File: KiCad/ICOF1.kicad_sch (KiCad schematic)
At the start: 40 parts, among them J1 USB C Connector, J2 JTAG_TC2030, SW1 Boot, U1 XC6206, U2 USBLC6-2SC6, U3 RP2040, U4 W25Q128JVS, Y1 12MHz

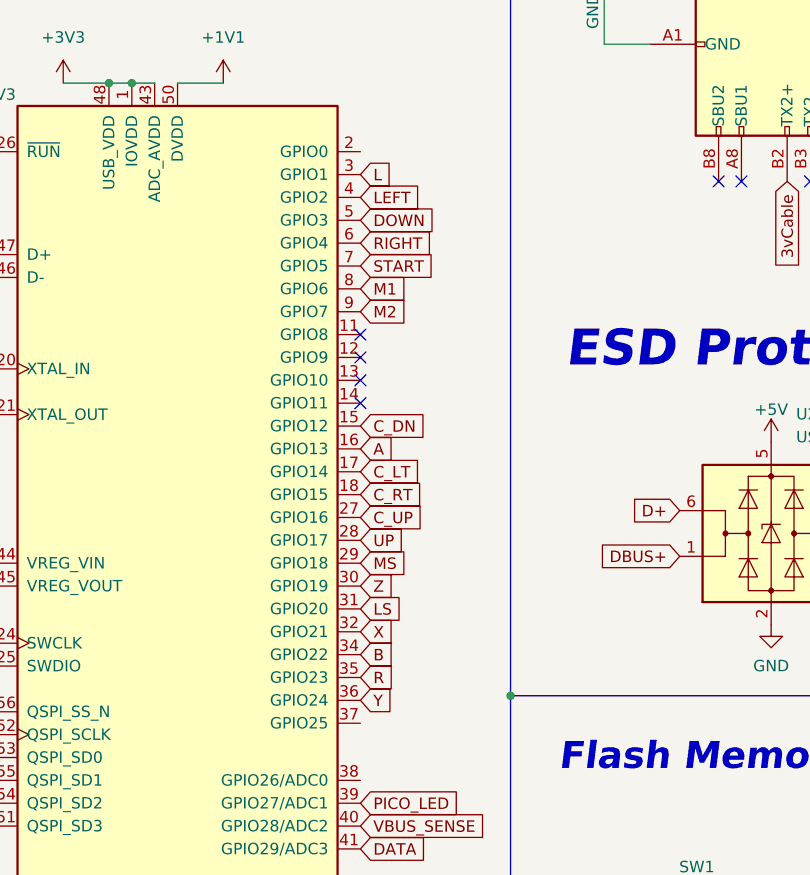
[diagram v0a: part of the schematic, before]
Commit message: fixed L and R, corrected sch pinout
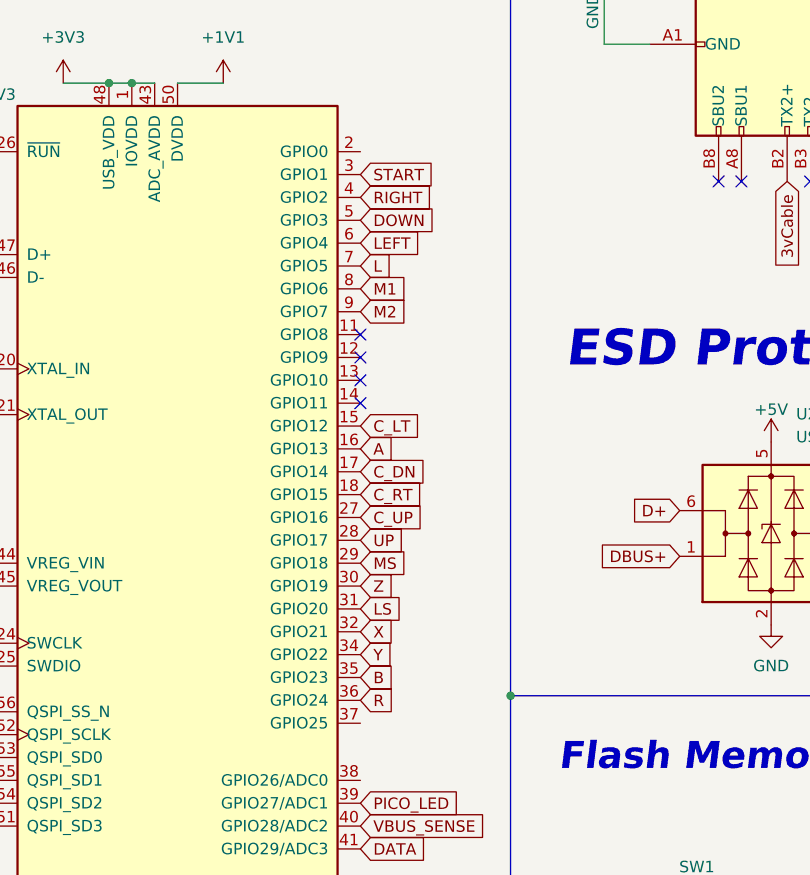
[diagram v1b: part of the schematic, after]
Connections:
- net B: now also U3.35 (GPIO23); no longer U3.34 (GPIO22)
- net C_DN: now also U3.17 (GPIO14); no longer U3.15 (GPIO12)
- net C_LT: now also U3.15 (GPIO12); no longer U3.17 (GPIO14)
- net L: now also U3.7 (GPIO5); no longer U3.3 (GPIO1)
- net LEFT: now also U3.6 (GPIO4); no longer U3.4 (GPIO2)
- net R: now also U3.36 (GPIO24); no longer U3.35 (GPIO23)
- net RIGHT: now also U3.4 (GPIO2); no longer U3.6 (GPIO4)
- net START: now also U3.3 (GPIO1); no longer U3.7 (GPIO5)
- net Y: now also U3.34 (GPIO22); no longer U3.36 (GPIO24)
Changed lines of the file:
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@@
     (effects (font (size 0.8 0.8)) (justify right bottom))
   )
-  (global_label "START" (shape input) (at 71.9648 61.214 0) (fields_autoplaced)
-    (effects (font (size 1.27 1.27)) (justify left))
-    (property "Intersheetrefs" "${INTERSHEET_REFS}" (at 79.8812 61.1346 0)
+  (global_label "L" (shape input) (at 71.9648 61.214 0) (fields_autoplaced)
+    (effects (font (size 1.27 1.27)) (justify left))
+    (property "Intersheetrefs" "${INTERSHEET_REFS}" (at 75.8987 61.214 0)
       (effects (font (size 1.27 1.27)) (justify left) hide)
     )
@@
     )
   )
-  (global_label "RIGHT" (shape input) (at 71.9648 58.674 0) (fields_autoplaced)
-    (effects (font (size 1.27 1.27)) (justify left))
-    (property "Intersheetrefs" "${INTERSHEET_REFS}" (at 79.8208 58.5946 0)
+  (global_label "LEFT" (shape input) (at 71.9648 58.674 0) (fields_autoplaced)
+    (effects (font (size 1.27 1.27)) (justify left))
+    (property "Intersheetrefs" "${INTERSHEET_REFS}" (at 79.1039 58.674 0)
       (effects (font (size 1.27 1.27)) (justify left) hide)
     )
@@
     )
   )
-  (global_label "L" (shape input) (at 71.9648 51.054 0) (fields_autoplaced)
-    (effects (font (size 1.27 1.27)) (justify left))
-    (property "Intersheetrefs" "${INTERSHEET_REFS}" (at 75.406 50.9746 0)
+  (global_label "START" (shape input) (at 71.9648 51.054 0) (fields_autoplaced)
+    (effects (font (size 1.27 1.27)) (justify left))
+    (property "Intersheetrefs" "${INTERSHEET_REFS}" (at 80.3739 51.054 0)
       (effects (font (size 1.27 1.27)) (justify left) hide)
     )
@@
     )
   )
-  (global_label "Y" (shape input) (at 71.9648 109.474 0) (fields_autoplaced)
-    (effects (font (size 1.27 1.27)) (justify left))
-    (property "Intersheetrefs" "${INTERSHEET_REFS}" (at 75.4665 109.3946 0)
+  (global_label "R" (shape input) (at 71.9648 109.474 0) (fields_autoplaced)
+    (effects (font (size 1.27 1.27)) (justify left))
+    (property "Intersheetrefs" "${INTERSHEET_REFS}" (at 76.1406 109.474 0)
       (effects (font (size 1.27 1.27)) (justify left) hide)
     )
@@
     )
   )
-  (global_label "C_DN" (shape input) (at 71.9648 78.994 0) (fields_autoplaced)
-    (effects (font (size 1.27 1.27)) (justify left))
-    (property "Intersheetrefs" "${INTERSHEET_REFS}" (at 79.216 78.9146 0)
-      (effects (font (size 1.27 1.27)) (justify left) hide)
-    )
-  )
-  (global_label "R" (shape input) (at 71.9648 106.934 0) (fields_autoplaced)
-    (effects (font (size 1.27 1.27)) (justify left))
-    (property "Intersheetrefs" "${INTERSHEET_REFS}" (at 75.6479 106.8546 0)
+  (global_label "C_LT" (shape input) (at 71.9648 78.994 0) (fields_autoplaced)
+    (effects (font (size 1.27 1.27)) (justify left))
+    (property "Intersheetrefs" "${INTERSHEET_REFS}" (at 79.1039 78.994 0)
+      (effects (font (size 1.27 1.27)) (justify left) hide)
+    )
+  )
+  (global_label "B" (shape input) (at 71.9648 106.934 0) (fields_autoplaced)
+    (effects (font (size 1.27 1.27)) (justify left))
+    (property "Intersheetrefs" "${INTERSHEET_REFS}" (at 76.1406 106.934 0)
       (effects (font (size 1.27 1.27)) (justify left) hide)
     )
@@
     )
   )
-  (global_label "LEFT" (shape input) (at 71.9648 53.594 0) (fields_autoplaced)
-    (effects (font (size 1.27 1.27)) (justify left))
-    (property "Intersheetrefs" "${INTERSHEET_REFS}" (at 78.6112 53.5146 0)
+  (global_label "RIGHT" (shape input) (at 71.9648 53.594 0) (fields_autoplaced)
+    (effects (font (size 1.27 1.27)) (justify left))
+    (property "Intersheetrefs" "${INTERSHEET_REFS}" (at 80.3135 53.594 0)
       (effects (font (size 1.27 1.27)) (justify left) hide)
     )
@@
     )
   )
-  (global_label "C_LT" (shape input) (at 71.9648 84.074 0) (fields_autoplaced)
-    (effects (font (size 1.27 1.27)) (justify left))
-    (property "Intersheetrefs" "${INTERSHEET_REFS}" (at 78.6112 83.9946 0)
+  (global_label "C_DN" (shape input) (at 71.9648 84.074 0) (fields_autoplaced)
+    (effects (font (size 1.27 1.27)) (justify left))
+    (property "Intersheetrefs" "${INTERSHEET_REFS}" (at 79.7087 84.074 0)
       (effects (font (size 1.27 1.27)) (justify left) hide)
     )
@@
     )
   )
-  (global_label "B" (shape input) (at 71.9648 104.394 0) (fields_autoplaced)
-    (effects (font (size 1.27 1.27)) (justify left))
-    (property "Intersheetrefs" "${INTERSHEET_REFS}" (at 75.6479 104.3146 0)
-      (effects (font (size 1.27 1.27)) (justify left) hide)
-    )
+  (global_label "Y" (shape input) (at 71.9648 104.394 0) (fields_autoplaced)
+    (effects (font (size 1.27 1.27)) (justify left))
+    (property "Intersheetrefs" "${INTERSHEET_REFS}" (at 75.9592 104.394 0)
+      (effects (font (size 1.27 1.27)) (justify left) hide)
+    )

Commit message: v1.4
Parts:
- added SW10, SW12, SW15, SW16, SW19, SW2, SW20, SW23, SW24, SW27, SW29, SW31, SW32, SW35, SW37, SW39, SW41, SW5, SW7, SW9: MX_SW_HS, marbastlib-mx:SW_MX_HS_1u, symbol marbastlib-mx:MX_SW_HS
- added SW11, SW13, SW14, SW17, SW18, SW21, SW22, SW25, SW26, SW28, SW3, SW30, SW33, SW34, SW36, SW38, SW4, SW40, SW6, SW8: MX_SW_solder, marbastlib-mx:SW_MX_1u, symbol marbastlib-mx:MX_SW_solder
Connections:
- net A: now also SW20.2, SW21.1
- net B: now also SW28.1, SW29.2
- net C_DN: now also SW16.2, SW17.1
- net C_LT: now also SW18.1, SW19.2
- net C_RT: now also SW24.2, SW25.1
- net C_UP: now also SW22.1, SW23.2
- net DOWN: now also SW6.2, SW7.1
- net GND: now also SW10.1, SW11.2, SW12.1, SW13.2, SW14.2, SW15.1, SW16.1, SW17.2, SW18.2, SW19.1, SW2.1, SW20.1, SW21.2, SW22.2, SW23.1, SW24.1, SW25.2, SW26.2, SW27.1, SW28.2, SW29.1, SW3.2, SW30.2, SW31.1, SW32.1, SW33.2, SW34.2, SW35.1, SW36.2, SW37.1, SW38.2, SW39.1, SW4.2, SW40.2, SW41.1, SW5.1, SW6.1, SW7.2, SW8.2, SW9.1
- net L: now also SW2.2, SW3.1
- net LEFT: now also SW4.1, SW5.2
- net LS: now also SW34.1, SW35.2
- net M1: now also SW10.2, SW11.1
- net M2: now also SW12.2, SW13.1
- net MS: now also SW38.1, SW39.2
- net R: now also SW26.1, SW27.2
- net RIGHT: now also SW8.1, SW9.2
- net START: now also SW14.1, SW15.2
- net UP: now also SW40.1, SW41.2
- net X: now also SW32.2, SW33.1
- net Y: now also SW30.1, SW31.2
- net Z: now also SW36.1, SW37.2
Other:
- removed sheet Buttons

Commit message: final final v1.2
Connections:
- net A: now also U3.17 (GPIO14); no longer U3.16 (GPIO13)
- net B: now also U3.38 (GPIO26/ADC0); no longer U3.35 (GPIO23)
- net C_DN: now also U3.18 (GPIO15); no longer U3.17 (GPIO14)
- net C_LT: now also U3.16 (GPIO13); no longer U3.15 (GPIO12)
- net C_RT: now also U3.27 (GPIO16); no longer U3.18 (GPIO15)
- net C_UP: now also U3.15 (GPIO12); no longer U3.27 (GPIO16)
- net DATA: now also U3.40 (GPIO28/ADC2); no longer U3.41 (GPIO29/ADC3)
- net PICO_LED: now also U3.37 (GPIO25); no longer U3.39 (GPIO27/ADC1)
- net R: now also U3.39 (GPIO27/ADC1); no longer U3.36 (GPIO24)
- net START: now also U3.2 (GPIO0); no longer U3.3 (GPIO1)
- net VBUS_SENSE: now also U3.41 (GPIO29/ADC3); no longer U3.40 (GPIO28/ADC2)
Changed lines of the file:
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@@
+    )
+  )
+  (global_label "VBUS_SENSE" (shape input) (at 71.9648 125.984 0) (fields_autoplaced)
+    (effects (font (size 1.27 1.27)) (justify left))
+    (property "Intersheetrefs" "${INTERSHEET_REFS}" (at 86.7843 125.984 0)
+      (effects (font (size 1.27 1.27)) (justify left) hide)
     )
   )
@@
     )
   )
+  (global_label "PICO_LED" (shape input) (at 71.9648 112.014 0) (fields_autoplaced)
+    (effects (font (size 1.27 1.27)) (justify left))
+    (property "Intersheetrefs" "${INTERSHEET_REFS}" (at 83.7606 112.014 0)
+      (effects (font (size 1.27 1.27)) (justify left) hide)
+    )
+  )
   (global_label "D+" (shape input) (at 21.114 59.944 180) (fields_autoplaced)
     (effects (font (size 1.27 1.27)) (justify right))
@@
     )
   )
+  (global_label "DATA" (shape input) (at 71.9648 123.444 0) (fields_autoplaced)
+    (effects (font (size 1.27 1.27)) (justify left))
+    (property "Intersheetrefs" "${INTERSHEET_REFS}" (at 78.7927 123.3646 0)
+      (effects (font (size 1.27 1.27)) (justify left) hide)
+    )
+  )
   (global_label "RIGHT" (shape input) (at 258.6482 133.1214 270) (fields_autoplaced)
     (effects (font (size 1.27 1.27)) (justify right))
@@
     )
   )
-  (global_label "START" (shape input) (at 71.9648 51.054 0) (fields_autoplaced)
-    (effects (font (size 1.27 1.27)) (justify left))
-    (property "Intersheetrefs" "${INTERSHEET_REFS}" (at 80.3739 51.054 0)
-      (effects (font (size 1.27 1.27)) (justify left) hide)
-    )
-  )
   (global_label "SD3" (shape input) (at 156.972 142.494 0) (fields_autoplaced)
     (effects (font (size 1.27 1.27)) (justify left))
@@
     )
   )
-  (global_label "R" (shape input) (at 71.9648 109.474 0) (fields_autoplaced)
-    (effects (font (size 1.27 1.27)) (justify left))
-    (property "Intersheetrefs" "${INTERSHEET_REFS}" (at 76.1406 109.474 0)
-      (effects (font (size 1.27 1.27)) (justify left) hide)
-    )
-  )
   (global_label "CS" (shape input) (at 130.302 134.874 90) (fields_autoplaced)
     (effects (font (size 1.27 1.27)) (justify left))
@@
     )
   )
+  (global_label "R" (shape input) (at 71.9648 120.904 0) (fields_autoplaced)
+    (effects (font (size 1.27 1.27)) (justify left))
+    (property "Intersheetrefs" "${INTERSHEET_REFS}" (at 76.1406 120.904 0)
+      (effects (font (size 1.27 1.27)) (justify left) hide)
+    )
+  )
   (global_label "SD3" (shape input) (at 31.3248 123.444 180) (fields_autoplaced)
     (effects (font (size 1.27 1.27)) (justify right))
@@
     )
   )
-  (global_label "PICO_LED" (shape input) (at 71.9648 120.904 0) (fields_autoplaced)
-    (effects (font (size 1.27 1.27)) (justify left))
-    (property "Intersheetrefs" "${INTERSHEET_REFS}" (at 83.7606 120.904 0)
-      (effects (font (size 1.27 1.27)) (justify left) hide)
-    )
-  )
-  (global_label "C_LT" (shape input) (at 71.9648 78.994 0) (fields_autoplaced)
-    (effects (font (size 1.27 1.27)) (justify left))
-    (property "Intersheetrefs" "${INTERSHEET_REFS}" (at 79.1039 78.994 0)
-      (effects (font (size 1.27 1.27)) (justify left) hide)
-    )
-  )
-  (global_label "B" (shape input) (at 71.9648 106.934 0) (fields_autoplaced)
-    (effects (font (size 1.27 1.27)) (justify left))
-    (property "Intersheetrefs" "${INTERSHEET_REFS}" (at 76.1406 106.934 0)
+  (global_label "C_UP" (shape input) (at 71.9648 78.994 0) (fields_autoplaced)
+    (effects (font (size 1.27 1.27)) (justify left))
+    (property "Intersheetrefs" "${INTERSHEET_REFS}" (at 79.7087 78.994 0)
       (effects (font (size 1.27 1.27)) (justify left) hide)
     )
@@
     )
   )
-  (global_label "A" (shape input) (at 71.9648 81.534 0) (fields_autoplaced)
-    (effects (font (size 1.27 1.27)) (justify left))
-    (property "Intersheetrefs" "${INTERSHEET_REFS}" (at 75.4665 81.4546 0)
+  (global_label "C_LT" (shape input) (at 71.9648 81.534 0) (fields_autoplaced)
+    (effects (font (size 1.27 1.27)) (justify left))
+    (property "Intersheetrefs" "${INTERSHEET_REFS}" (at 79.1039 81.534 0)
       (effects (font (size 1.27 1.27)) (justify left) hide)
     )
@@
     )
   )
-  (global_label "C_DN" (shape input) (at 71.9648 84.074 0) (fields_autoplaced)
-    (effects (font (size 1.27 1.27)) (justify left))
-    (property "Intersheetrefs" "${INTERSHEET_REFS}" (at 79.7087 84.074 0)
+  (global_label "A" (shape input) (at 71.9648 84.074 0) (fields_autoplaced)
+    (effects (font (size 1.27 1.27)) (justify left))
+    (property "Intersheetrefs" "${INTERSHEET_REFS}" (at 75.9592 84.074 0)
       (effects (font (size 1.27 1.27)) (justify left) hide)
     )
@@
     )
   )
-  (global_label "DATA" (shape input) (at 71.9648 125.984 0) (fields_autoplaced)
-    (effects (font (size 1.27 1.27)) (justify left))
-    (property "Intersheetrefs" "${INTERSHEET_REFS}" (at 78.7927 125.9046 0)
-      (effects (font (size 1.27 1.27)) (justify left) hide)
-    )
-  )
-  (global_label "C_RT" (shape input) (at 71.9648 86.614 0) (fields_autoplaced)
-    (effects (font (size 1.27 1.27)) (justify left))
-    (property "Intersheetrefs" "${INTERSHEET_REFS}" (at 78.8531 86.5346 0)
+  (global_label "B" (shape input) (at 71.9648 118.364 0) (fields_autoplaced)
+    (effects (font (size 1.27 1.27)) (justify left))
+    (property "Intersheetrefs" "${INTERSHEET_REFS}" (at 76.1406 118.364 0)
+      (effects (font (size 1.27 1.27)) (justify left) hide)
+    )
+  )
+  (global_label "C_DN" (shape input) (at 71.9648 86.614 0) (fields_autoplaced)
+    (effects (font (size 1.27 1.27)) (justify left))
+    (property "Intersheetrefs" "${INTERSHEET_REFS}" (at 79.7087 86.614 0)
+      (effects (font (size 1.27 1.27)) (justify left) hide)
+    )
+  )
+  (global_label "START" (shape input) (at 71.9648 48.514 0) (fields_autoplaced)
+    (effects (font (size 1.27 1.27)) (justify left))
+    (property "Intersheetrefs" "${INTERSHEET_REFS}" (at 80.3739 48.514 0)
       (effects (font (size 1.27 1.27)) (justify left) hide)
     )
@@
     )
   )
-  (global_label "C_UP" (shape input) (at 71.9648 89.154 0) (fields_autoplaced)
-    (effects (font (size 1.27 1.27)) (justify left))
-    (property "Intersheetrefs" "${INTERSHEET_REFS}" (at 79.216 89.0746 0)
+  (global_label "C_RT" (shape input) (at 71.9648 89.154 0) (fields_autoplaced)
+    (effects (font (size 1.27 1.27)) (justify left))
+    (property "Intersheetrefs" "${INTERSHEET_REFS}" (at 79.3458 89.154 0)
       (effects (font (size 1.27 1.27)) (justify left) hide)
     )
@@
       (effects (font (size 1.27 1.27)) (justify left) hide)
     )
-  )
-  (global_label "VBUS_SENSE" (shape input) (at 71.9648 123.444 0) (fields_autoplaced)
-    (effects (font (size 1.27 1.27)) (justify left))
-    (property "Intersheetrefs" "${INTERSHEET_REFS}" (at 86.7843 123.444 0)
-      (effects (font (size 1.27 1.27)) (justify left) hide)
-    )
